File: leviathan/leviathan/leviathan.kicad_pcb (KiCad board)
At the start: 2 copper layers, 240 x 145 mm, 26 parts, among them SW1 SW_Push, SW10 SW_Push, SW11 SW_Push, SW12 SW_Push, SW13 SW_Push, SW14 SW_Push, SW15 SW_Push, SW16 SW_Push, SW17 SW_Push, SW18 SW_Push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

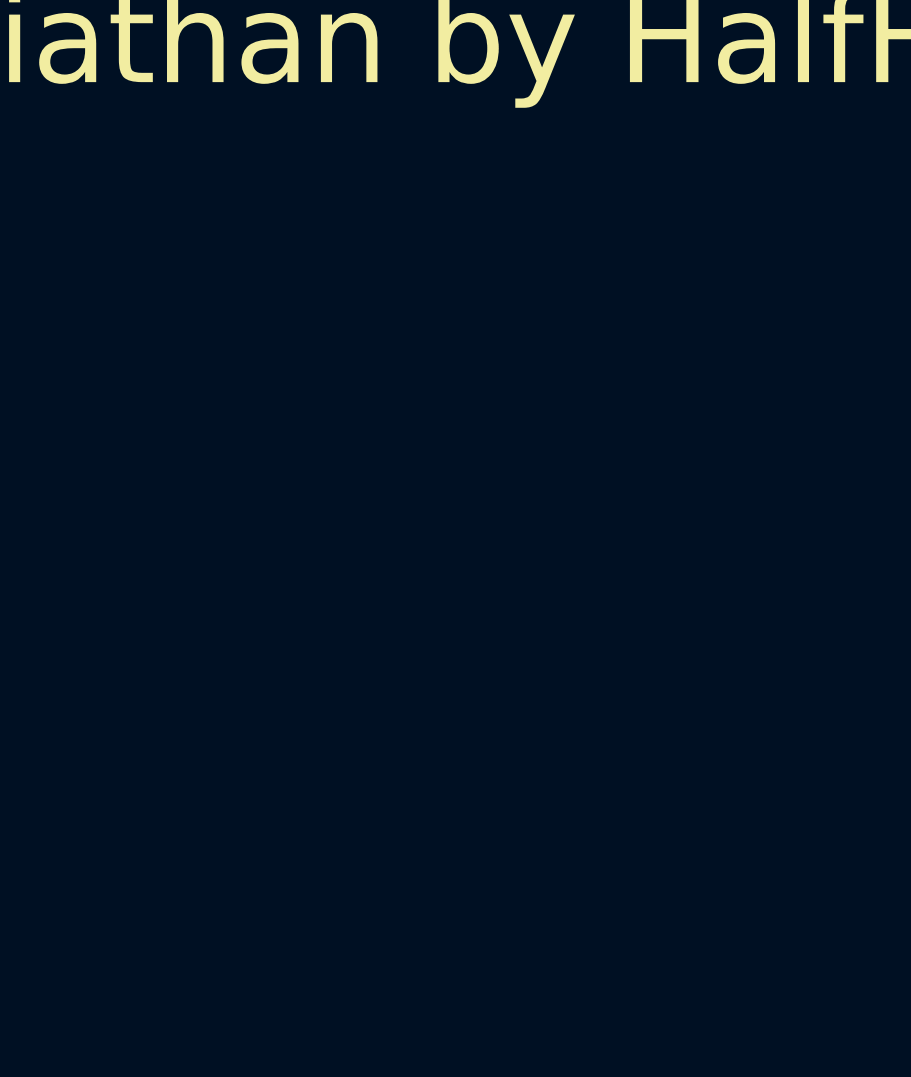
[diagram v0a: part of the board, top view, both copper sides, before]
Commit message: Added ground fill and fixed PCB issues from schematic update
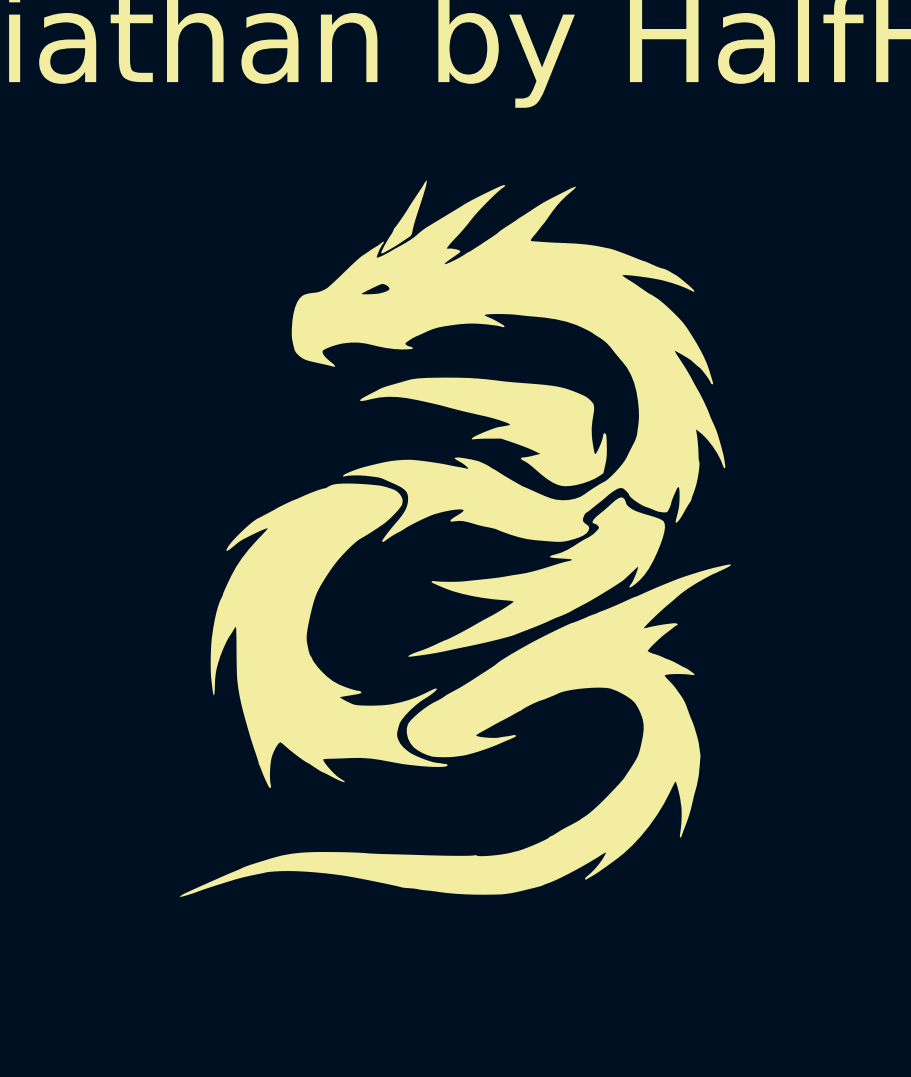
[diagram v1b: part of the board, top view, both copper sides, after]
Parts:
- added leviathan-logo: , LOGO, F.Cu at (250.7, 132.4)
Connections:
- A1 pad 14: LEFT -> OPT4
- A1 pad 15: OPT1 -> LEFT
- A1 pad 16: OPT2 -> OPT3
- A1 pad 17: OPT3 -> OPT1
- A1 pad 18: OPT4 -> OPT2
- A1 pad 3: L1 -> L2
- A1 pad 4: L2 -> L1
